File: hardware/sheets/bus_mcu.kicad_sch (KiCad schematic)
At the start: 56 parts, among them M1 Core2350B (0MB PSRAM), U10 74HC161, U11 74HC161, U12 74HCT165, U13 74LVC245A, U14 74HCT244, U15 74HCT244, U16 74HCT244, U17 74HCT04, U18 74HC08, U2 74LVC245A, U3 74LVC245A, U4 74LVC245A, U5 74LVC245A, U6 74LVC245A, U7 74HC161, U8 74HC161, U9 74HC161

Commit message: Parts: footprints for all components, close 6 LCSC map gaps, check_parts.py
- mxsch.py emits the Footprint property from component props (was
  hard-coded empty); parts.py entries now carry a verified KiCad
  footprint, applied at build time alongside the LCSC number.
- Map keys fixed to match placed values: USB_PROG, SS34, LED (PicoGUS),
  APS6404L, CB3T3257/45 -- every combo across all sheets + cards now
  resolves (130 combos, 455 netlist components, all with footprints).
- Package corrections from JLC DB re-check: RTL8019AS is QFP-100 14x20
  P0.65 (not TQFP); C2897411 female header is a 2x10 strip -- fine for
  Core2350B, Pico needs 2x 1x20 (noted in jlcpcb-sourcing.md).
- 10 mini-xt:* placeholder footprints mark parts whose land pattern is
  authored at layout from the EasyEDA data (CH224K, magnetics, RJ45,
  HDMI, CF socket, ISA slot, switches, Core2350B PGA).
- New tools/check_parts.py: fails on unmapped combos, missing fp
  fields, or footprints absent from the installed KiCad libs.

Co-Authored-By: Claude Fable 5 <noreply@anthropic.com>
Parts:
- C1, C10, C11, C12, C13, C14, C15, C16, C17, C2, C6, C7, C8, C9: footprint (none) -> Capacitor_SMD:C_0603_1608Metric
- C3: footprint (none) -> Capacitor_SMD:C_0805_2012Metric
- D1: footprint (none) -> Diode_SMD:D_SMA; LCSC Part Num (none) -> C8678
- M1: footprint (none) -> mini-xt:Core2350B_PGA
- R1, R10, R11, R12, R13, R14, R15, R16, R17, R18, R2, R25, R26, R27, R28, R3, R4, R5, R6, R7, R8, R9: footprint (none) -> Resistor_SMD:R_0603_1608Metric
- U10, U11, U12, U7, U8, U9: footprint (none) -> Package_SO:SOIC-16_3.9x9.9mm_P1.27mm
- U13, U2, U3, U4, U5, U6: footprint (none) -> Package_SO:TSSOP-20_4.4x6.5mm_P0.65mm
- U14, U15, U16: footprint (none) -> Package_SO:SOIC-20W_7.5x12.8mm_P1.27mm
- U17, U18: footprint (none) -> Package_SO:SOIC-14_3.9x8.7mm_P1.27mm
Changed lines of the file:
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@@
 			)
 		)
-		(property "Footprint" ""
+		(property "Footprint" "mini-xt:Core2350B_PGA"
 			(at 101.6 152.4 0)
 			(effects
@@
 			)
 		)
-		(property "Footprint" ""
+		(property "Footprint" "Diode_SMD:D_SMA"
+			(at 40.64 116.84 0)
+			(effects
+				(font
+					(size 1.27 1.27)
+				)
+				(hide yes)
+			)
+		)
+		(property "LCSC Part Num" "C8678"
 			(at 40.64 116.84 0)
 			(effects
@@
 			)
 		)
-		(property "Footprint" ""
+		(property "Footprint" "Package_SO:TSSOP-20_4.4x6.5mm_P0.65mm"
 			(at 200.66 76.2 0)
 			(effects
@@
 			)
 		)
-		(property "Footprint" ""
+		(property "Footprint" "Package_SO:TSSOP-20_4.4x6.5mm_P0.65mm"
 			(at 200.66 152.4 0)
 			(effects
@@
 			)
 		)
-		(property "Footprint" ""
+		(property "Footprint" "Package_SO:TSSOP-20_4.4x6.5mm_P0.65mm"
 			(at 281.94 76.2 0)
 			(effects
@@
 			)
 		)
-		(property "Footprint" ""
+		(property "Footprint" "Package_SO:TSSOP-20_4.4x6.5mm_P0.65mm"
 			(at 358.14 76.2 0)
 			(effects
@@
 			)
 		)
-		(property "Footprint" ""
+		(property "Footprint" "Package_SO:TSSOP-20_4.4x6.5mm_P0.65mm"
 			(at 281.94 152.4 0)
 			(effects
@@
 			)
 		)
-		(property "Footprint" ""
+		(property "Footprint" "Package_SO:TSSOP-20_4.4x6.5mm_P0.65mm"
 			(at 358.14 152.4 0)
 			(effects
@@
 			)
 		)
-		(property "Footprint" ""
+		(property "Footprint" "Resistor_SMD:R_0603_1608Metric"
 			(at 340.36 172.72 0)
 			(effects
@@
 			)
 		)
-		(property "Footprint" ""
+		(property "Footprint" "Package_SO:SOIC-16_3.9x9.9mm_P1.27mm"
 			(at 60.96 271.78 0)
 			(effects
@@
 			)
 		)
-		(property "Footprint" ""
+		(property "Footprint" "Package_SO:SOIC-16_3.9x9.9mm_P1.27mm"
 			(at 127 271.78 0)
 			(effects
@@
 			)
 		)
-		(property "Footprint" ""
+		(property "Footprint" "Package_SO:SOIC-16_3.9x9.9mm_P1.27mm"
 			(at 193.04 271.78 0)
 			(effects
@@
 			)
 		)
-		(property "Footprint" ""
+		(property "Footprint" "Package_SO:SOIC-16_3.9x9.9mm_P1.27mm"
 			(at 259.08 271.78 0)
 			(effects
@@
 			)
 		)
-		(property "Footprint" ""
+		(property "Footprint" "Package_SO:SOIC-16_3.9x9.9mm_P1.27mm"
 			(at 325.12 271.78 0)
 			(effects
@@
 			)
 		)
-		(property "Footprint" ""
+		(property "Footprint" "Package_SO:SOIC-14_3.9x8.7mm_P1.27mm"
 			(at 398.78 203.2 0)
 			(effects
@@
 			)
 		)
-		(property "Footprint" ""
+		(property "Footprint" "Capacitor_SMD:C_0603_1608Metric"
 			(at 398.78 182.88 0)
 			(effects
@@
 			)
 		)
-		(property "Footprint" ""
+		(property "Footprint" "Package_SO:SOIC-14_3.9x8.7mm_P1.27mm"
 			(at 236.22 233.68 0)
 			(effects
@@
 			)
 		)
-		(property "Footprint" ""
+		(property "Footprint" "Package_SO:SOIC-20W_7.5x12.8mm_P1.27mm"
 			(at 281.94 233.68 0)
 			(effects
@@
 			)
 		)
-		(property "Footprint" ""
+		(property "Footprint" "Package_SO:SOIC-20W_7.5x12.8mm_P1.27mm"
 			(at 327.66 233.68 0)
 			(effects
@@
 			)
 		)
-		(property "Footprint" ""
+		(property "Footprint" "Package_SO:SOIC-20W_7.5x12.8mm_P1.27mm"
 			(at 373.38 233.68 0)
 			(effects
@@
 			)
 		)
-		(property "Footprint" ""
+		(property "Footprint" "Package_SO:SOIC-16_3.9x9.9mm_P1.27mm"
 			(at 200.66 233.68 0)
 			(effects
@@
 			)
 		)
-		(property "Footprint" ""
+		(property "Footprint" "Resistor_SMD:R_0603_1608Metric"
 			(at 86.36 25.4 0)
 			(effects
@@
 			)
 		)
-		(property "Footprint" ""
+		(property "Footprint" "Resistor_SMD:R_0603_1608Metric"
 			(at 101.6 25.4 0)
 			(effects
@@
 			)
 		)
-		(property "Footprint" ""
+		(property "Footprint" "Resistor_SMD:R_0603_1608Metric"
 			(at 116.84 25.4 0)
 			(effects
@@
 			)
 		)
-		(property "Footprint" ""
+		(property "Footprint" "Resistor_SMD:R_0603_1608Metric"
 			(at 132.08 25.4 0)
 			(effects
@@
 			)
 		)
-		(property "Footprint" ""
+		(property "Footprint" "Resistor_SMD:R_0603_1608Metric"
 			(at 147.32 25.4 0)
 			(effects
@@
 			)
 		)
-		(property "Footprint" ""
+		(property "Footprint" "Resistor_SMD:R_0603_1608Metric"
 			(at 162.56 25.4 0)
 			(effects
@@
 			)
 		)
-		(property "Footprint" ""
+		(property "Footprint" "Resistor_SMD:R_0603_1608Metric"
 			(at 177.8 25.4 0)
 			(effects
@@
 			)
 		)
-		(property "Footprint" ""
+		(property "Footprint" "Resistor_SMD:R_0603_1608Metric"
 			(at 193.04 25.4 0)
 			(effects
@@
 			)
 		)
-		(property "Footprint" ""
+		(property "Footprint" "Resistor_SMD:R_0603_1608Metric"
 			(at 208.28 25.4 0)
 			(effects
@@
 			)
 		)
-		(property "Footprint" ""
+		(property "Footprint" "Resistor_SMD:R_0603_1608Metric"
 			(at 223.52 25.4 0)
 			(effects
@@
 			)
 		)
-		(property "Footprint" ""
+		(property "Footprint" "Resistor_SMD:R_0603_1608Metric"
 			(at 238.76 25.4 0)
 			(effects
@@
 			)
 		)
-		(property "Footprint" ""
+		(property "Footprint" "Resistor_SMD:R_0603_1608Metric"
 			(at 254 25.4 0)
 			(effects
@@
 			)
 		)
-		(property "Footprint" ""
+		(property "Footprint" "Resistor_SMD:R_0603_1608Metric"
 			(at 269.24 25.4 0)
 			(effects
@@
 			)
 		)
-		(property "Footprint" ""
+		(property "Footprint" "Resistor_SMD:R_0603_1608Metric"
 			(at 284.48 25.4 0)
 			(effects
@@
 			)
 		)
-		(property "Footprint" ""
+		(property "Footprint" "Resistor_SMD:R_0603_1608Metric"
 			(at 299.72 25.4 0)
 			(effects
@@
 			)
 		)
-		(property "Footprint" ""
+		(property "Footprint" "Resistor_SMD:R_0603_1608Metric"
 			(at 314.96 25.4 0)
 			(effects
@@
 			)
 		)
-		(property "Footprint" ""
+		(property "Footprint" "Resistor_SMD:R_0603_1608Metric"
 			(at 330.2 25.4 0)
 			(effects
@@
 			)
 		)
-		(property "Footprint" ""
+		(property "Footprint" "Resistor_SMD:R_0603_1608Metric"
 			(at 345.44 25.4 0)
 			(effects
@@
 			)
 		)
-		(property "Footprint" ""
+		(property "Footprint" "Resistor_SMD:R_0603_1608Metric"
 			(at 360.68 25.4 0)
 			(effects
@@
 			)
 		)
-		(property "Footprint" ""
+		(property "Footprint" "Resistor_SMD:R_0603_1608Metric"
 			(at 375.92 25.4 0)
 			(effects
@@
 			)
 		)
-		(property "Footprint" ""
+		(property "Footprint" "Resistor_SMD:R_0603_1608Metric"
 			(at 391.16 25.4 0)
 			(effects
@@
 			)
 		)
-		(property "Footprint" ""
+		(property "Footprint" "Capacitor_SMD:C_0603_1608Metric"
 			(at 40.64 50.8 0)
 			(effects
@@
 			)
 		)
-		(property "Footprint" ""
+		(property "Footprint" "Capacitor_SMD:C_0603_1608Metric"
 			(at 55.88 50.8 0)
 			(effects
@@
 			)
 		)
-		(property "Footprint" ""
+		(property "Footprint" "Capacitor_SMD:C_0805_2012Metric"
 			(at 71.12 50.8 0)
 			(effects
@@
 			)
 		)
-		(property "Footprint" ""
+		(property "Footprint" "Capacitor_SMD:C_0603_1608Metric"
 			(at 190.5 40.64 0)
 			(effects
@@
 			)
 		)
-		(property "Footprint" ""
+		(property "Footprint" "Capacitor_SMD:C_0603_1608Metric"
 			(at 271.78 40.64 0)
 			(effects
@@
 			)
 		)
-		(property "Footprint" ""
+		(property "Footprint" "Capacitor_SMD:C_0603_1608Metric"
 			(at 350.52 40.64 0)
 			(effects
@@
 			)
 		)
-		(property "Footprint" ""
+		(property "Footprint" "Capacitor_SMD:C_0603_1608Metric"
 			(at 50.8 220.98 0)
 			(effects
@@
 			)
 		)
-		(property "Footprint" ""
+		(property "Footprint" "Capacitor_SMD:C_0603_1608Metric"
 			(at 190.5 198.12 0)
 			(effects
@@
 			)
 		)
-		(property "Footprint" ""
+		(property "Footprint" "Capacitor_SMD:C_0603_1608Metric"
 			(at 281.94 213.36 0)
 			(effects
@@
 			)
 		)
-		(property "Footprint" ""
+		(property "Footprint" "Capacitor_SMD:C_0603_1608Metric"
 			(at 327.66 213.36 0)
 			(effects
@@
 			)
 		)
-		(property "Footprint" ""
+		(property "Footprint" "Capacitor_SMD:C_0603_1608Metric"
 			(at 373.38 213.36 0)
 			(effects
@@
 			)
 		)
-		(property "Footprint" ""
+		(property "Footprint" "Capacitor_SMD:C_0603_1608Metric"
 			(at 251.46 213.36 0)
 			(effects
@@
 			)
 		)
-		(property "Footprint" ""
+		(property "Footprint" "Capacitor_SMD:C_0603_1608Metric"
 			(at 35.56 220.98 0)
 			(effects
@@
 			)
 		)
-		(property "Footprint" ""
+		(property "Footprint" "Capacitor_SMD:C_0603_1608Metric"
 			(at 20.32 220.98 0)
 			(effects

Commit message: bus_mcu: direct 3.3V bus GPIOs (LVC245s+DIR logic deleted); EXT IRQ/DRQ scan
Deleted all six 74LVC245A (data/strobes/address+BALE/AEN-TC) and their DIR
logic; each MCU GPIO now sits on its 3.3V bus net 1:1 (RP2350B is 5V-tolerant
and tri-states natively). Freed GPIO43 (ex-DATADIR) -> EXP_DDIR. Moved the
'165 IRQ collector, the counter '244 output-enable stage and its inverter to
+3V3 (74HC values). Added a 2x 74HC165 EXT scan chain (U19/U20) for the
expansion-port EXT_IRQ2-8/EXT_DRQ1-3 lines. Kept U14-U16 '244s (deviation
from the brief): they are the '163 counter's only tri-state, not level
shifters -- deleting them would fight cpu_core's '573 latches on A0-A19.

Co-Authored-By: Claude Fable 5 <noreply@anthropic.com>
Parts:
- removed C1, C10, C11, C12, C13, C14, C15, C16, C17, C2, C6, C7, C8, C9: 100nF, Capacitor_SMD:C_0603_1608Metric, symbol Device:C
- removed C3: 10uF, Capacitor_SMD:C_0805_2012Metric, symbol Device:C
- removed U13, U2, U3, U4, U5, U6: 74LVC245A, Package_SO:TSSOP-20_4.4x6.5mm_P0.65mm, symbol mini-xt:74LVC245A
- added C18, C19: 100nF, Capacitor_SMD:C_0603_1608Metric, symbol Device:C
- added R10, R11, R12, R13, R14, R15, R17, R18, R25, R26, R30, R31, R32, R33, R34, R35, R36, R37, R38: 10k, Resistor_SMD:R_0603_1608Metric, symbol Device:R
- added U12, U19, U20: 74HC165, Package_SO:SOIC-16_3.9x9.9mm_P1.27mm, symbol mini-xt:74HCT165
- added U7: 74HC161, Package_SO:SOIC-16_3.9x9.9mm_P1.27mm, symbol mini-xt:74HCT163
- C1: renamed from R10; value 10k -> 100nF; footprint Resistor_SMD:R_0603_1608Metric -> Capacitor_SMD:C_0603_1608Metric; symbol Device:R -> Device:C; LCSC Part Num C25804 -> C14663
- C10: renamed from R14; value 10k -> 100nF; footprint Resistor_SMD:R_0603_1608Metric -> Capacitor_SMD:C_0603_1608Metric; symbol Device:R -> Device:C; LCSC Part Num C25804 -> C14663
- C11: renamed from U7; value 74HC161 -> 100nF; footprint Package_SO:SOIC-16_3.9x9.9mm_P1.27mm -> Capacitor_SMD:C_0603_1608Metric; symbol mini-xt:74HCT163 -> Device:C; LCSC Part Num C5610 -> C14663
- C12: renamed from R15; value 10k -> 100nF; footprint Resistor_SMD:R_0603_1608Metric -> Capacitor_SMD:C_0603_1608Metric; symbol Device:R -> Device:C; LCSC Part Num C25804 -> C14663
- C13: renamed from R16; value 10k -> 100nF; footprint Resistor_SMD:R_0603_1608Metric -> Capacitor_SMD:C_0603_1608Metric; symbol Device:R -> Device:C; LCSC Part Num C25804 -> C14663
- C14: renamed from R17; value 10k -> 100nF; footprint Resistor_SMD:R_0603_1608Metric -> Capacitor_SMD:C_0603_1608Metric; symbol Device:R -> Device:C; LCSC Part Num C25804 -> C14663
- C15: renamed from R18; value 10k -> 100nF; footprint Resistor_SMD:R_0603_1608Metric -> Capacitor_SMD:C_0603_1608Metric; symbol Device:R -> Device:C; LCSC Part Num C25804 -> C14663
- C16: renamed from R25; value 10k -> 100nF; footprint Resistor_SMD:R_0603_1608Metric -> Capacitor_SMD:C_0603_1608Metric; symbol Device:R -> Device:C; LCSC Part Num C25804 -> C14663
- C17: renamed from R26; value 10k -> 100nF; footprint Resistor_SMD:R_0603_1608Metric -> Capacitor_SMD:C_0603_1608Metric; symbol Device:R -> Device:C; LCSC Part Num C25804 -> C14663
- C2: renamed from R11; value 10k -> 100nF; footprint Resistor_SMD:R_0603_1608Metric -> Capacitor_SMD:C_0603_1608Metric; symbol Device:R -> Device:C; LCSC Part Num C25804 -> C14663
- C3: renamed from R12; value 10k -> 10uF; footprint Resistor_SMD:R_0603_1608Metric -> Capacitor_SMD:C_0805_2012Metric; symbol Device:R -> Device:C; LCSC Part Num C25804 -> C15850
- C9: renamed from R13; value 10k -> 100nF; footprint Resistor_SMD:R_0603_1608Metric -> Capacitor_SMD:C_0603_1608Metric; symbol Device:R -> Device:C; LCSC Part Num C25804 -> C14663
- R29: renamed from U12; value 74HCT165 -> 10k; footprint Package_SO:SOIC-16_3.9x9.9mm_P1.27mm -> Resistor_SMD:R_0603_1608Metric; symbol mini-xt:74HCT165 -> Device:R; LCSC Part Num C456131 -> C25804
- U14, U15, U16: value 74HCT244 -> 74HC244; LCSC Part Num C5978 -> C52140409
- U17: value 74HCT04 -> 74HC04; LCSC Part Num C672096 -> C86613
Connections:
- net MA0 is gone; now on net A0: M1.9 (GPIO8)
- net MA1 is gone; now on net A1: M1.10 (GPIO9)
- net MA2 is gone; now on net A2: M1.11 (GPIO10)
- net MA3 is gone; now on net A3: M1.12 (GPIO11)
- net MA4 is gone; now on net A4: M1.13 (GPIO12)
- net MA5 is gone; now on net A5: M1.14 (GPIO13)
- net MA6 is gone; now on net A6: M1.15 (GPIO14)
- net MA7 is gone; now on net A7: M1.16 (GPIO15)
- net MD4 is gone; now on net D4: M1.5 (GPIO4), U10.3 (D0), U8.3 (D0)
- net MD5 is gone; now on net D5: M1.6 (GPIO5), U10.4 (D1), U8.4 (D1)
- net MD6 is gone; now on net D6: M1.7 (GPIO6), U10.5 (D2), U8.5 (D2)
- net MD7 is gone; now on net D7: M1.8 (GPIO7), U10.6 (D3), U8.6 (D3)
- net M_BALE is gone; now on net BALE: M1.21 (GPIO20)
- net M_IOR is gone; now on net ~{IOR}: M1.17 (GPIO16)
- net M_IOW is gone; now on net ~{IOW}: M1.18 (GPIO17)
- net M_MEMR is gone; now on net ~{MEMR}: M1.19 (GPIO18)
- net M_MEMW is gone; now on net ~{MEMW}: M1.20 (GPIO19)
- net +5V: no longer C3.1, C9.1, R2.1, R29.16 (VCC), R3.1, U14.20 (VCC), U15.20 (VCC), U16.19 (2OE), U16.20 (VCC), U17.14 (VCC)
- net AEN: now also M1.22 (GPIO21), R1.2
- net CA0: now also U7.14 (Q0); no longer C11.14 (Q0)
- net CA1: now also U7.13 (Q1); no longer C11.13 (Q1)
- net CA2: now also U7.12 (Q2); no longer C11.12 (Q2)
- net CA3: now also U7.11 (Q3); no longer C11.11 (Q3)
- net CNT_CLK: now also U7.2 (CP); no longer C11.2 (CP)
- net CNT_LD0: now also U7.9 (~{PE}); no longer C11.9 (~{PE})
- net CNT_RUN: now also U7.7 (CEP); no longer C11.7 (CEP)
- net CNT_TC0: now also U7.15 (TC); no longer C11.15 (TC)
- net D0: now also M1.1 (GPIO0), U11.3 (D0), U9.3 (D0), U7.3 (D0)
- net D1: now also M1.2 (GPIO1), U11.4 (D1), U9.4 (D1), U7.4 (D1)
- net D2: now also M1.3 (GPIO2), U11.5 (D2), U9.5 (D2), U7.5 (D2)
- net D3: now also M1.4 (GPIO3), U11.6 (D3), U9.6 (D3), U7.6 (D3)
- net DRQ2: now also R14.2; no longer C10.2
- net DRQ3: now also R15.2; no longer C12.2
- net GND: now also C1.2, C10.2, C11.2, C12.2, C13.2, C14.2, C15.2, C16.2, C17.2, C2.2, C3.1, C3.2, C9.1, C9.2, R1.1, R29.1, C18.2, C19.2, R10.1, R11.1, R14.1, R15.1, R17.1, R18.1, R25.1, R26.1, R30.1, R31.1, R32.1, R33.1, R34.1, R35.1, R36.1, R37.1, R38.1, U12.15 (~{CE}), U12.8 (GND), U19.15 (~{CE}), U19.6 (D7), U19.8 (GND), U20.10 (DS), U20.14 (D3), U20.15 (~{CE}), U20.3 (D4), U20.4 (D5), U20.5 (D6), U20.6 (D7), U20.8 (GND), U7.1 (~{MR}), U7.10 (CET), U7.16 (VCC), U7.8 (GND); no longer C10.1, C11.10 (CET), C11.16 (VCC), C11.8 (GND), C12.1, C13.1, C14.1, C15.1, R1.2, R29.10 (DS), R29.15 (~{CE}), R29.8 (GND)
- net HLDA: now also R18.2; no longer C15.2
- net IRQ14: now also R11.2, U12.6 (D7); no longer C2.2, R29.6 (D7)
- net IRQ2: now also U12.11 (D0); no longer R29.11 (D0)
- net IRQ3: now also U12.12 (D1); no longer R29.12 (D1)
- net IRQ4: now also U12.13 (D2); no longer R29.13 (D2)
- net IRQ5: now also U12.14 (D3); no longer R29.14 (D3)
- net IRQ6: now also U12.3 (D4); no longer R29.3 (D4)
- net IRQ7: now also U12.4 (D5); no longer R29.4 (D5)
- net IRQ8: now also R10.2, U12.5 (D6); no longer C1.2, R29.5 (D6)
- net IRQ_CLK: now also U12.2 (CP), U19.2 (CP), U20.2 (CP); no longer R29.2 (CP)
- net IRQ_LOAD: now also U12.1 (~{PL}), U19.1 (~{PL}), U20.1 (~{PL}); no longer R29.1 (~{PL})
- net IRQ_SER: now also U12.9 (Q7); no longer R29.9 (Q7)
- net TC: now also M1.36 (GPIO35), R17.2
- net ~{CPURESET}: now also R25.2; no longer C16.2
- net ~{DACK1}: now also R26.2; no longer C17.2
- net ~{DACK2}: now also R12.2; no longer C3.2
- net ~{DACK3}: now also R13.2; no longer C9.2
- net DATADIR renamed EXP_DDIR
- net EXP_DDIR: no longer C13.2
- removed net MD0: C11.3 (D0), M1.1 (GPIO0), U11.3 (D0), U9.3 (D0)
- removed net MD1: C11.4 (D1), M1.2 (GPIO1), U11.4 (D1), U9.4 (D1)
- removed net MD2: C11.5 (D2), M1.3 (GPIO2), U11.5 (D2), U9.5 (D2)
- removed net MD3: C11.6 (D3), M1.4 (GPIO3), U11.6 (D3), U9.6 (D3)
- removed net M_AEN: M1.22 (GPIO21), R1.1
- removed net M_TC: C14.2, M1.36 (GPIO35)
- new net +3V3: C10.1, C12.1, C13.1, C14.1, C15.1, C18.1, C19.1, R12.1, R13.1, R2.1, R3.1, U12.16 (VCC), U14.20 (VCC), U15.20 (VCC), U16.19 (2OE), U16.20 (VCC), U17.14 (VCC), U19.16 (VCC), U20.16 (VCC)
- new net EXT_DRQ1: R29.2, U20.11 (D0)
- new net EXT_DRQ2: R30.2, U20.12 (D1)
- new net EXT_DRQ3: R31.2, U20.13 (D2)
- new net EXT_IRQ2: R32.2, U19.11 (D0)
- new net EXT_IRQ3: R33.2, U19.12 (D1)
- new net EXT_IRQ4: R34.2, U19.13 (D2)
- new net EXT_IRQ5: R35.2, U19.14 (D3)
- new net EXT_IRQ6: R36.2, U19.3 (D4)
- new net EXT_IRQ7: R37.2, U19.4 (D5)
- new net EXT_IRQ8: R38.2, U19.5 (D6)
- new net IRQ_CHAIN1: U12.10 (DS), U19.9 (Q7)
- new net IRQ_CHAIN2: U19.10 (DS), U20.9 (Q7)
- no-connect marks 47 -> 23
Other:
- note added: "3.3V bus: data/addr/strobe/BALE/AEN/TC wired GPIO<->bus directly (no '245s);"
- note added: "master/slave role = firmware tri-state. R1/R17/R18 idle AEN/TC/HLDA during MCU Hi-Z."
- note added: "§5.2 IRQ+EXT scan: 3x 74HC165 -> 3 MCU pins; order U12(IRQ)->U19(EXT_IRQ)->U20(EXT_DRQ)"
- note removed: "U3-U5 address+BALE = fixed sense; U13 AEN/TC = fixed drive (R1 idles AEN low)"
- note removed: "U6 strobes DIR = HLDA (bus role, §5.2); DATADIR = data read/write dir;"
- note removed: "§5.2 IRQ collector: 74HCT165 -> 3 MCU pins, 8-bit shift (D0-D6=IRQ2-8, D7=IRQ14)"

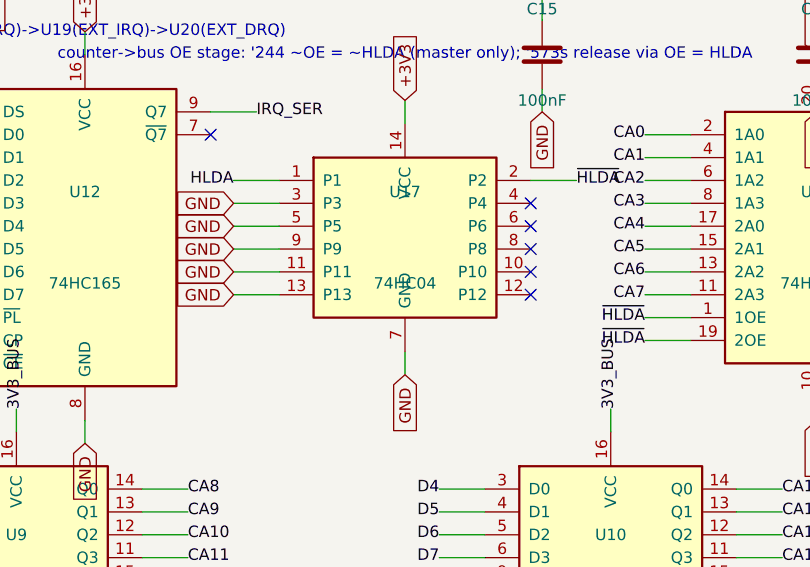
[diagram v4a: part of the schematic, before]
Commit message: 3.3V redesign: final-review fix wave (6 findings)
Reviewer-verified fixes, all at the generator level + regenerated outputs:

1. (Critical) bus_mcu U17 '04 @+3V3 had the V20's 5V HLDA on its input ->
   value-override to 74LVC04A (5V-tolerant input; parts.py binds C282341).
2. network R7 (AEN_CHIP park) +5V -> +3V3: it also feeds U5's '138 @+3V3;
   RTL8019AS AEN is 5V-TTL so 3.3V still reads high.
3. sidecar buf244(): tie unused '244 A inputs to GND, no_connect the Y
   outputs (U1105: 6 spare, U1108: 7) -- no floating always-enabled inputs.
4. MAX3241s (both com_port instances) +5V -> +3V3; charge-pump caps to the
   datasheet 3.0-3.6V column (all 0.1uF). Removes the 5V-R*OUT-into-3.3V-UART
   receiver path; com_port now has no +5V rail.
5. V20 READY/HOLD re-buffered through cpu_core U13's 3 spare '04 gates (zero
   package cost). READY = 2 gates (non-inverting), single-driver (no fold).
   HOLD = 1 inverting gate -> FIRMWARE MUST DRIVE HOLD ACTIVE-LOW at GPIO25
   (mxbus HOLD name intact). U13 nudged to clear a stub collision with U12.
6. Docs census + staleness: rewrote the 5V census to post-fix reality across
   CLAUDE.md, spec, design doc, README, irq-io-map (IRQ8 soft-PIC/undriven),
   parts.py header notes.

Build exit 0; check_parts 0 problems; all five sheets validate with zero
structural violations. Netlist evidence in questions-*.md.

Co-Authored-By: Claude Fable 5 <noreply@anthropic.com>
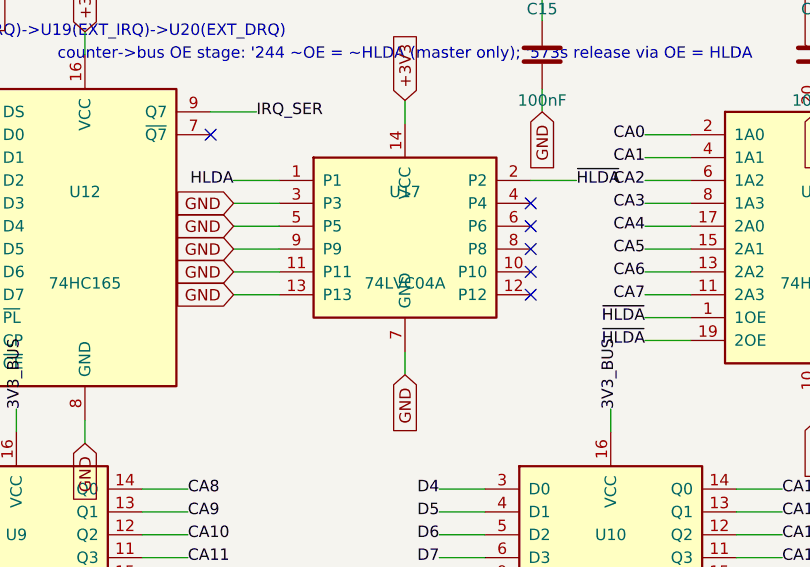
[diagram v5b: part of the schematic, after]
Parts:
- U17: value 74HC04 -> 74LVC04A; LCSC Part Num C86613 -> C282341
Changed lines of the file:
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@@
 			)
 		)
-		(property "Value" "74HC04"
+		(property "Value" "74LVC04A"
 			(at 236.22 238.76 0)
 			(effects
@@
 			)
 		)
-		(property "LCSC Part Num" "C86613"
+		(property "LCSC Part Num" "C282341"
 			(at 236.22 233.68 0)
 			(effects
